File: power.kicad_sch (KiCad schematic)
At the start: 40 parts, among them J201 USBC, Q201 2N7002, Q202 BSS84, SW201 PWR_ON, U201 MAX17043G+T, U202 MCP73831-3-OT, U203 LM3670MF

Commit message: Update component footprint selection
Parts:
- C210: footprint Capacitor_Tantalum_SMD:CP_EIA-6032-28_Kemet-C_HandSolder -> Capacitor_Tantalum_SMD:CP_EIA-7343-31_Kemet-D_HandSolder
- L201: footprint Inductor_SMD_Wurth:L_Wurth_WE-LQSH-2010 -> Inductor_SMD_Wurth:L_Wurth_WE-LQSH-2512
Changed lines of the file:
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@@
 			)
 		)
-		(property "Footprint" "Capacitor_Tantalum_SMD:CP_EIA-6032-28_Kemet-C_HandSolder"
+		(property "Footprint" "Capacitor_Tantalum_SMD:CP_EIA-7343-31_Kemet-D_HandSolder"
 			(at 242.2652 135.89 0)
 			(effects
@@
 			)
 		)
-		(property "Footprint" "Inductor_SMD_Wurth:L_Wurth_WE-LQSH-2010"
+		(property "Footprint" "Inductor_SMD_Wurth:L_Wurth_WE-LQSH-2512"
 			(at 231.14 124.46 0)
 			(effects
@@
 			)
 		)
-		(property "Datasheet" "~"
+		(property "Datasheet" ""
 			(at 231.14 124.46 0)
 			(effects

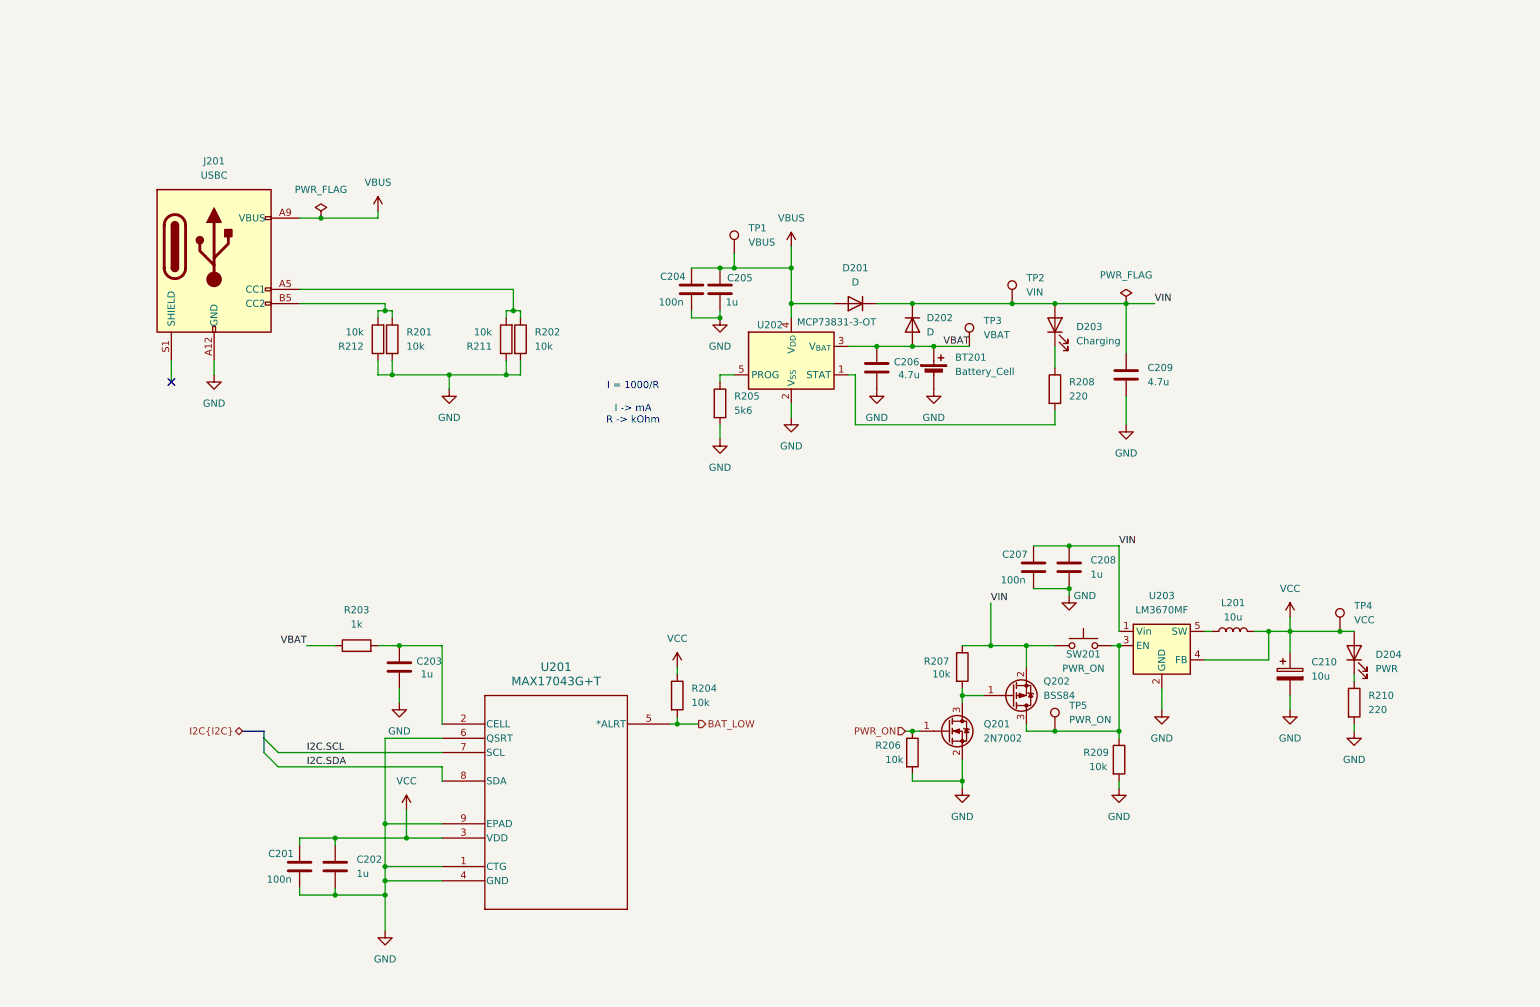
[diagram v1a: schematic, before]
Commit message: Use new regulator
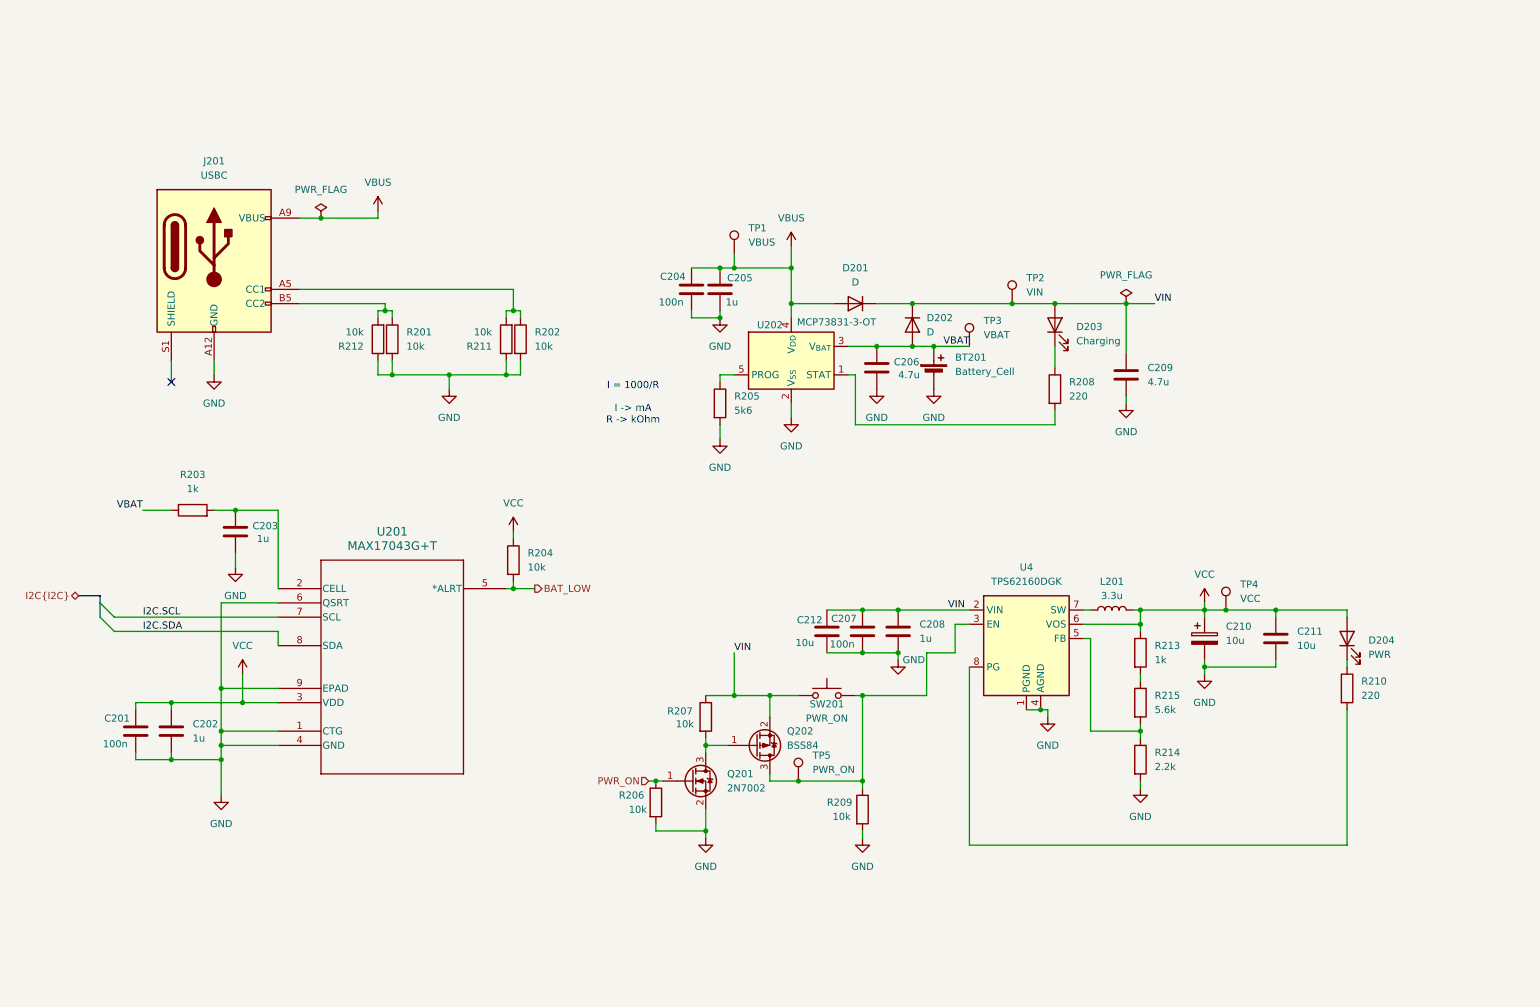
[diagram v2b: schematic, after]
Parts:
- removed U203: LM3670MF, Package_TO_SOT_SMD:TSOT-23-5_HandSoldering, symbol Regulator_Switching:LM3670MF
- added C211, C212: 10u, Capacitor_SMD:C_1206_3216Metric_Pad1.33x1.80mm_HandSolder, symbol Device:C
- added R213: 1k, Resistor_SMD:R_1206_3216Metric_Pad1.30x1.75mm_HandSolder, symbol Device:R
- added R214: 2.2k, Resistor_SMD:R_1206_3216Metric_Pad1.30x1.75mm_HandSolder, symbol Device:R
- added R215: 5.6k, Resistor_SMD:R_1206_3216Metric_Pad1.30x1.75mm_HandSolder, symbol Device:R
- added U4: TPS62160DGK, Package_SO:MSOP-8_3x3mm_P0.65mm, symbol Regulator_Switching:TPS62160DGK
- L201: value 10u -> 3.3u
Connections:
- net GND: now also C211.2, C212.2, R214.2, U4.1 (PGND), U4.4 (AGND); no longer R210.2
- net VCC: now also C211.1, R213.1, U4.6 (VOS)
- net VIN: now also C212.1, U4.2 (VIN)
- net at Q202.3 (D), R209.1, SW201.2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: now also U4.3 (EN)
- net at L201.1: now also U4.7 (SW)
- new net: R213.2, R215.1
- new net: R210.2, U4.8 (PG)
- new net: R214.1, R215.2, U4.5 (FB)
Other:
- moved on the sheet: C201, C202, C203, C207, C208, C210, D204, L201, Q201, Q202, R203, R204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

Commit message: Using buck-boost regulator
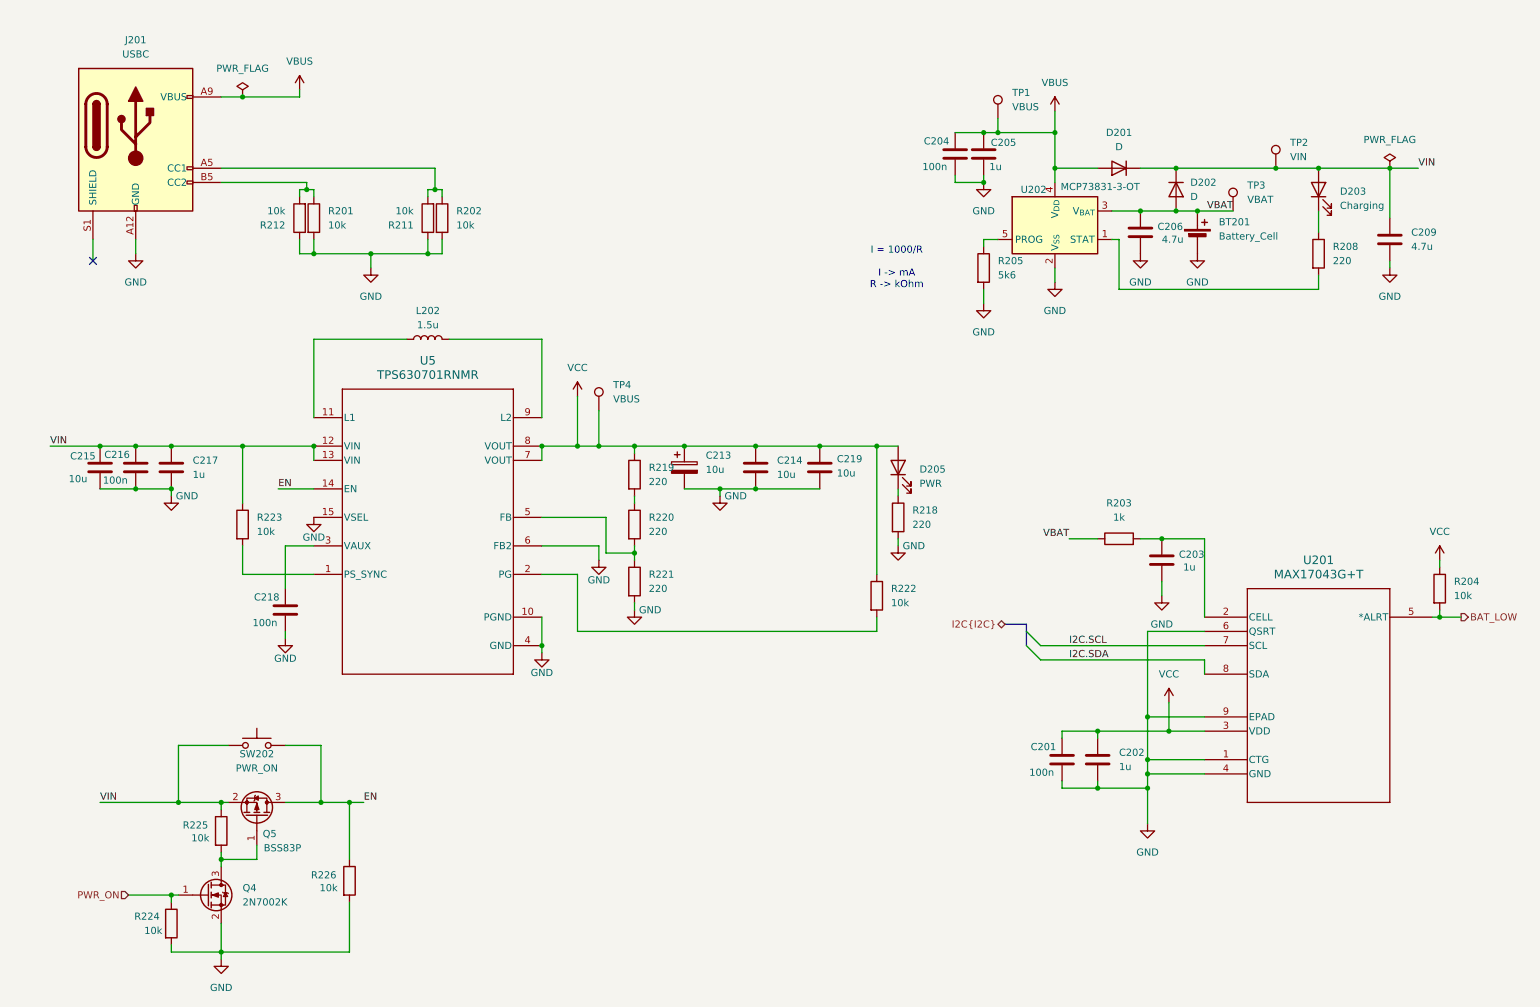
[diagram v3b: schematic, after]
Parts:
- removed C207: 100n, Capacitor_SMD:C_1206_3216Metric_Pad1.33x1.80mm_HandSolder, symbol Device:C
- removed C208: 1u, Capacitor_SMD:C_1206_3216Metric_Pad1.33x1.80mm_HandSolder, symbol Device:C
- removed C210: 10u, Capacitor_Tantalum_SMD:CP_EIA-7343-31_Kemet-D_HandSolder, symbol Device:C_Polarized
- removed C211, C212: 10u, Capacitor_SMD:C_1206_3216Metric_Pad1.33x1.80mm_HandSolder, symbol Device:C
- removed D204: PWR, LED_SMD:LED_1206_3216Metric_Pad1.42x1.75mm_HandSolder, symbol Device:LED
- removed L201: 3.3u, Inductor_SMD_Wurth:L_Wurth_WE-LQSH-2512, symbol Device:L
- removed Q201: 2N7002, Package_TO_SOT_SMD:SOT-23W_Handsoldering, symbol Transistor_FET:2N7002
- removed Q202: BSS84, Package_TO_SOT_SMD:SOT-23W_Handsoldering, symbol Transistor_FET:BSS84
- removed R206, R207, R209: 10k, Resistor_SMD:R_1206_3216Metric_Pad1.30x1.75mm_HandSolder, symbol Device:R
- removed R210: 220, Resistor_SMD:R_1206_3216Metric_Pad1.30x1.75mm_HandSolder, symbol Device:R
- removed R213: 1k, Resistor_SMD:R_1206_3216Metric_Pad1.30x1.75mm_HandSolder, symbol Device:R
- removed R214: 2.2k, Resistor_SMD:R_1206_3216Metric_Pad1.30x1.75mm_HandSolder, symbol Device:R
- removed R215: 5.6k, Resistor_SMD:R_1206_3216Metric_Pad1.30x1.75mm_HandSolder, symbol Device:R
- removed SW201: PWR_ON, Button_Switch_SMD:SW_SPST_PTS647_Sx38, symbol Switch:SW_Push
- removed TP5: PWR_ON, TestPoint:TestPoint_Pad_D1.0mm, symbol Connector:TestPoint
- removed U4: TPS62160DGK, Package_SO:MSOP-8_3x3mm_P0.65mm, symbol Regulator_Switching:TPS62160DGK
- added C213: 10u, Capacitor_Tantalum_SMD:CP_EIA-7343-31_Kemet-D_HandSolder, symbol Device:C_Polarized
- added C214, C215, C219: 10u, Capacitor_SMD:C_1206_3216Metric_Pad1.33x1.80mm_HandSolder, symbol Device:C
- added C216, C218: 100n, Capacitor_SMD:C_1206_3216Metric_Pad1.33x1.80mm_HandSolder, symbol Device:C
- added C217: 1u, Capacitor_SMD:C_1206_3216Metric_Pad1.33x1.80mm_HandSolder, symbol Device:C
- added D205: PWR, LED_SMD:LED_1206_3216Metric_Pad1.42x1.75mm_HandSolder, symbol Device:LED
- added L202: 1.5u, Inductor_SMD_Wurth:L_Wurth_WE-LQSH-2512, symbol Device:L
- added Q4: 2N7002K, Package_TO_SOT_SMD:SOT-23, symbol Transistor_FET:2N7002K
- added Q5: BSS83P, Package_TO_SOT_SMD:SOT-23, symbol Transistor_FET:BSS83P
- added R218, R219, R220, R221: 220, Resistor_SMD:R_1206_3216Metric_Pad1.30x1.75mm_HandSolder, symbol Device:R
- added R222, R223, R224, R225, R226: 10k, Resistor_SMD:R_1206_3216Metric_Pad1.30x1.75mm_HandSolder, symbol Device:R
- added SW202: PWR_ON, Button_Switch_SMD:SW_SPST_PTS647_Sx38, symbol Switch:SW_Push
- added U5: TPS630701RNMR, lib:TPS63070, symbol TPS63070:TPS630701RNMR
- TP4: value VCC -> VBUS
- U201: footprint lib:21-0174B_MXM -> lib:MAX17043
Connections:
- net GND: now also C213.2, C214.2, C215.2, C216.2, C217.2, C218.2, C219.2, Q4.2 (S), R218.2, R221.2, R224.2, R226.2, U5.10 (PGND), U5.15 (VSEL), U5.4 (GND), U5.6 (FB2)
- net PWR_ON: now also Q4.1 (G), R224.1
- net VCC: now also C213.1, C214.1, C219.1, D205.2 (A), R219.1, R222.1, U5.7 (VOUT), U5.8 (VOUT)
- net VIN: now also C215.1, C216.1, C217.1, Q5.2 (S), R223.1, R225.1, SW202.1, U5.12 (VIN), U5.13 (VIN)
- new net: D205.1 (K), R218.1
- new net: C218.1, U5.3 (VAUX)
- new net: R223.2, U5.1 (PS_SYNC)
- new net: L202.1, U5.11 (L1)
- new net: R222.2, U5.2 (PG)
- new net: R220.2, R221.1, U5.5 (FB)
- new net: L202.2, U5.9 (L2)
- new net: Q4.3 (D), Q5.1 (G), R225.2
- new net: R219.2, R220.1
- new net EN: Q5.3 (D), R226.1, SW202.2, U5.14 (EN)
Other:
- moved on the sheet: BT201, C201, C202, C203, C204, C205, C206, C209, D201, D202, D203, J201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

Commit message: Page reordering
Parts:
- added TP12: EN, TestPoint:TestPoint_Pad_D1.0mm, symbol Connector:TestPoint
- added TP5: ~{PG}, TestPoint:TestPoint_Pad_D1.0mm, symbol Connector:TestPoint
- R219: value 220 -> 10k
- R220: value 220 -> 1k
- R221: value 220 -> 2.2k
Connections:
- net EN: now also TP12.1
- net at R222.2, U5.2 (PG): now also TP5.1
- net at R220.2, R221.1: no longer U5.5 (FB)
- net at R219.2, R220.1: now also U5.5 (FB)
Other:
- moved on the sheet: R220
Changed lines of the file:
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@@
 	)
 	(junction
-		(at 124.46 110.49)
-		(diameter 0)
-		(color 0 0 0 0)
-	)
-	(junction
 		(at 157.48 91.44)
 		(diameter 0)
@@
 	)
 	(junction
+		(at 124.46 101.6)
+		(diameter 0)
+		(color 0 0 0 0)
+	)
+	(junction
 		(at 68.58 154.94)
 		(diameter 0)
@@
 	)
 	(junction
+		(at 144.78 124.46)
+		(diameter 0)
+		(color 0 0 0 0)
+	)
+	(junction
 		(at 77.47 57.15)
 		(diameter 0)
@@
 	(wire
 		(pts
-			(xy 73.66 154.94) (xy 76.2 154.94)
+			(xy 73.66 154.94) (xy 80.01 154.94)
 		)
 		(stroke
@@
 	(wire
 		(pts
+			(xy 113.03 104.14) (xy 107.95 104.14)
+		)
+		(stroke
+			(width 0)
+			(type default)
+		)
+	)
+	(wire
+		(pts
 			(xy 133.35 91.44) (xy 146.05 91.44)
 		)
@@
 	(wire
 		(pts
-			(xy 124.46 111.76) (xy 124.46 110.49)
+			(xy 124.46 101.6) (xy 124.46 102.87)
 		)
 		(stroke
@@
 	(wire
 		(pts
-			(xy 88.9 41.91) (xy 50.8 41.91)
-		)
-		(stroke
-			(width 0)
-			(type default)
-		)
-	)
-	(wire
-		(pts
-			(xy 107.95 91.44) (xy 107.95 93.98)
+			(xy 113.03 101.6) (xy 113.03 104.14)
 		)
 		(stroke
@@
 	(wire
 		(pts
-			(xy 210.82 63.5) (xy 246.38 63.5)
+			(xy 88.9 41.91) (xy 50.8 41.91)
 		)
 		(stroke
@@
 	(wire
 		(pts
-			(xy 119.38 110.49) (xy 124.46 110.49)
+			(xy 107.95 91.44) (xy 107.95 93.98)
 		)
 		(stroke
@@
 	(wire
 		(pts
-			(xy 119.38 104.14) (xy 119.38 110.49)
+			(xy 210.82 63.5) (xy 246.38 63.5)
 		)
 		(stroke
@@
 	(wire
 		(pts
+			(xy 124.46 110.49) (xy 124.46 111.76)
+		)
+		(stroke
+			(width 0)
+			(type default)
+		)
+	)
+	(wire
+		(pts
 			(xy 88.9 45.72) (xy 90.17 45.72)
 		)
@@
 	(wire
 		(pts
-			(xy 107.95 104.14) (xy 119.38 104.14)
+			(xy 113.03 101.6) (xy 124.46 101.6)
 		)
 		(stroke
@@
 	(wire
 		(pts
+			(xy 144.78 124.46) (xy 167.64 124.46)
+		)
+		(stroke
+			(width 0)
+			(type default)
+		)
+	)
+	(wire
+		(pts
 			(xy 226.06 132.08) (xy 226.06 129.54)
 		)
@@
 	(wire
 		(pts
-			(xy 124.46 109.22) (xy 124.46 110.49)
-		)
-		(stroke
-			(width 0)
-			(type default)
-		)
-	)
-	(wire
-		(pts
-			(xy 114.3 124.46) (xy 167.64 124.46)
+			(xy 114.3 124.46) (xy 144.78 124.46)
 		)
 		(stroke
@@
 	)
 	(label "EN"
-		(at 76.2 154.94 0)
+		(at 80.01 154.94 0)
 		(effects
 			(font
@@
 	)
 	(symbol
+		(lib_id "Connector:TestPoint")
+		(at 73.66 154.94 0)
+		(unit 1)
+		(exclude_from_sim no)
+		(in_bom yes)
+		(on_board yes)
+		(dnp no)
+		(property "Reference" "TP12"
+			(at 76.2 150.3679 0)
+			(effects
+				(font
+					(size 1.27 1.27)
+				)
+				(justify left)
+			)
+		)
+		(property "Value" "EN"
+			(at 76.2 152.9079 0)
+			(effects
+				(font
+					(size 1.27 1.27)
+				)
+				(justify left)
+			)
+		)
+		(property "Footprint" "TestPoint:TestPoint_Pad_D1.0mm"
+			(at 78.74 154.94 0)
+			(effects
+				(font
+					(size 1.27 1.27)
+				)
+				(hide yes)
+			)
+		)
+		(property "Datasheet" "~"
+			(at 78.74 154.94 0)
+			(effects
+				(font
+					(size 1.27 1.27)
+				)
+				(hide yes)
+			)
+		)
+		(property "Description" "test point"
+			(at 73.66 154.94 0)
+			(effects
+				(font
+					(size 1.27 1.27)
+				)
+				(hide yes)
+			)
+		)
+		(pin "1"
+		)
+		(instances
+			(project "LifeCounter"
+				(path "/16b3e55a-9d75-49bf-a6fe-25414eb3d7da/8f87360a-db94-4899-a1b3-392efb8a6c91"
+					(reference "TP12")
+					(unit 1)
+				)
+			)
+		)
+	)
+	(symbol
 		(lib_id "power:VCC")
 		(at 114.3 82.55 0)
@@
 			)
 		)
-		(property "Datasheet" "MAX17043G+T"
+		(property "Datasheet" "https://www.analog.com/media/en/technical-documentation/data-sheets/max17043-max17044.pdf"
 			(at 226.06 121.92 0)
 			(effects
@@
 	)
 	(symbol
+		(lib_id "Connector:TestPoint")
+		(at 144.78 124.46 0)
+		(unit 1)
+		(exclude_from_sim no)
+		(in_bom yes)
+		(on_board yes)
+		(dnp no)
+		(fields_autoplaced yes)
+		(property "Reference" "TP5"
+			(at 147.32 119.8879 0)
+			(effects
+				(font
+					(size 1.27 1.27)
+				)
+				(justify left)
+			)
+		)
+		(property "Value" "~{PG}"
+			(at 147.32 122.4279 0)
+			(effects
+				(font
+					(size 1.27 1.27)
+				)
+				(justify left)
+			)
+		)
+		(property "Footprint" "TestPoint:TestPoint_Pad_D1.0mm"
+			(at 149.86 124.46 0)
+			(effects
+				(font
+					(size 1.27 1.27)
+				)
+				(hide yes)
+			)
+		)
+		(property "Datasheet" "~"
+			(at 149.86 124.46 0)
+			(effects
+				(font
+					(size 1.27 1.27)
+				)
+				(hide yes)
+			)
+		)
+		(property "Description" "test point"
+			(at 144.78 124.46 0)
+			(effects
+				(font
+					(size 1.27 1.27)
+				)
+				(hide yes)
+			)
+		)
+		(pin "1"
+		)
+		(instances
+			(project "LifeCounter"
+				(path "/16b3e55a-9d75-49bf-a6fe-25414eb3d7da/8f87360a-db94-4899-a1b3-392efb8a6c91"
+					(reference "TP5")
+					(unit 1)
+				)
+			)
+		)
+	)
+	(symbol
 		(lib_id "power:GND")
 		(at 124.46 120.65 0)
@@
 			)
 		)
-		(property "Datasheet" "TPS630701RNMR"
+		(property "Datasheet" "https://www.ti.com/lit/gpn/TPS63070"
 			(at 87.63 106.68 0)
 			(effects
@@
 			)
 		)
-		(property "Value" "220"
+		(property "Value" "2.2k"
 			(at 127 116.8399 0)
 			(effects
@@
 			)
 		)
-		(property "Value" "220"
+		(property "Value" "10k"
 			(at 127 97.7899 0)
 			(effects
@@
 	(symbol
 		(lib_id "Device:R")
-		(at 124.46 105.41 0)
+		(at 124.46 106.68 0)
 		(unit 1)
 		(exclude_from_sim no)
@@
 		(fields_autoplaced yes)
 		(property "Reference" "R220"
-			(at 127 104.1399 0)
+			(at 127 105.4099 0)
 			(effects
 				(font
@@
 			)
 		)
-		(property "Value" "220"
-			(at 127 106.6799 0)
+		(property "Value" "1k"
+			(at 127 107.9499 0)
 			(effects
 				(font
@@
 		)
 		(property "Footprint" "Resistor_SMD:R_1206_3216Metric_Pad1.30x1.75mm_HandSolder"
-			(at 122.682 105.41 90)
+			(at 122.682 106.68 90)
 			(effects
 				(font
@@
 		)
 		(property "Datasheet" "~"
-			(at 124.46 105.41 0)
+			(at 124.46 106.68 0)
 			(effects
 				(font
@@
 		)
 		(property "Description" "Resistor"
-			(at 124.46 105.41 0)
+			(at 124.46 106.68 0)
 			(effects
 				(font
